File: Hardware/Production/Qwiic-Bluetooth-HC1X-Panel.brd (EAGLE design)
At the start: 97.3 x 97.3 mm, 492 parts, among them J1 ISP, J10 PIO, J11 ISP, J12 Qwiic-L, J13 Qwiic-R, J14 I2C, J15 PIO, J16 ISP, J17 Qwiic-L, J18 Qwiic-R, J19 I2C, J2 Qwiic-L, J20 PIO, J21 ISP, J22 Qwiic-L, J23 Qwiic-R, J24 I2C, J25 PIO, J26 ISP, J27 Qwiic-L, J28 Qwiic-R, J29 I2C, J3 Qwiic-R, J30 PIO, J31 ISP, J32 Qwiic-L, J33 Qwiic-R, J34 I2C, J35 PIO, J36 ISP, J37 Qwiic-L, J38 Qwiic-R, J39 I2C, J4 I2C, J40 PIO, J41 ISP, J42 Qwiic-L, J43 Qwiic-R, J44 I2C, J45 PIO, J5 PIO, J6 ISP, J7 Qwiic-L, J8 Qwiic-R, J9 I2C, U1 ATTiny85-Arduino, U10 ATTiny85-Arduino, U11 HM-17, U12 ATTiny85-Arduino, U13 HM-17, U14 ATTiny85-Arduino, U15 HM-17, U16 ATTiny85-Arduino, U17 HM-17, U18 ATTiny85-Arduino, U2 HM-17, U3 HM-17, U4 ATTiny85-Arduino, U5 HM-17, U6 ATTiny85-Arduino, U7 HM-17, U8 ATTiny85-Arduino, U9 HM-17

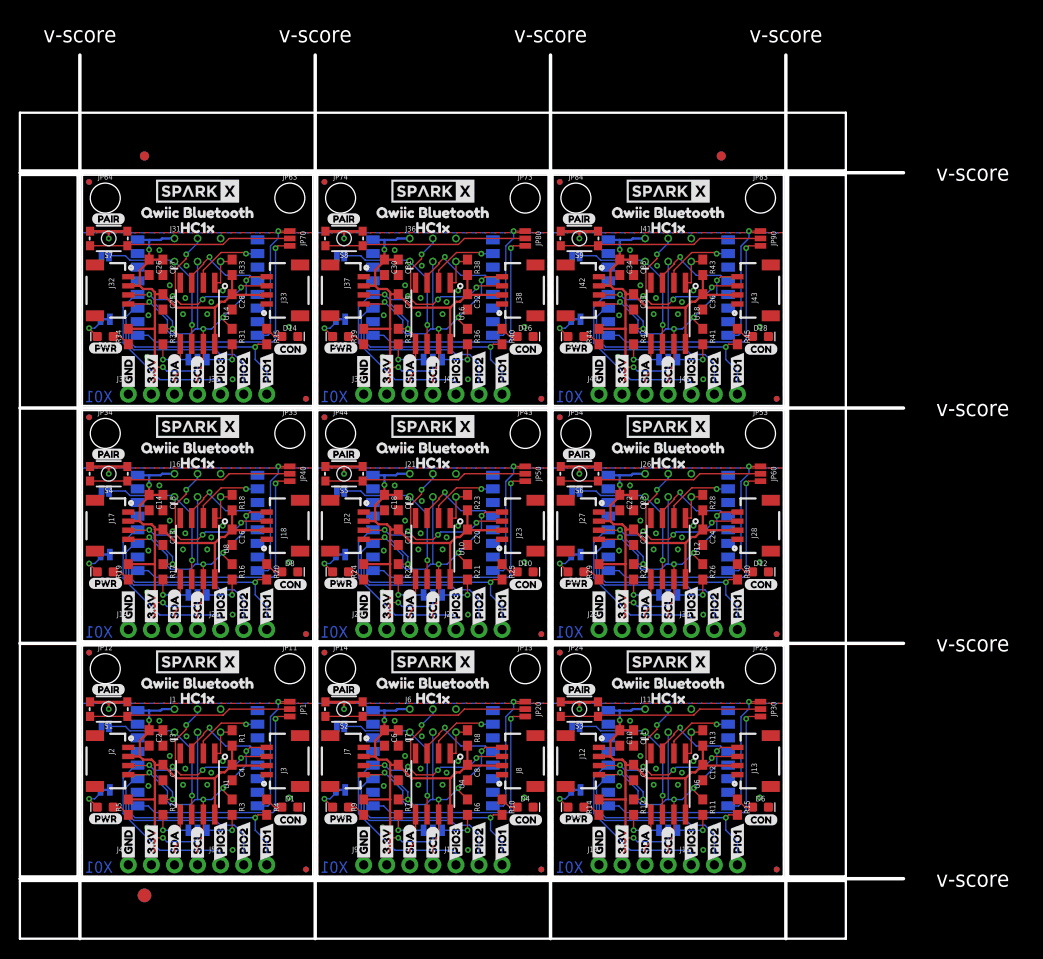
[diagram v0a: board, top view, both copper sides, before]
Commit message: Pushing production panel for x02.
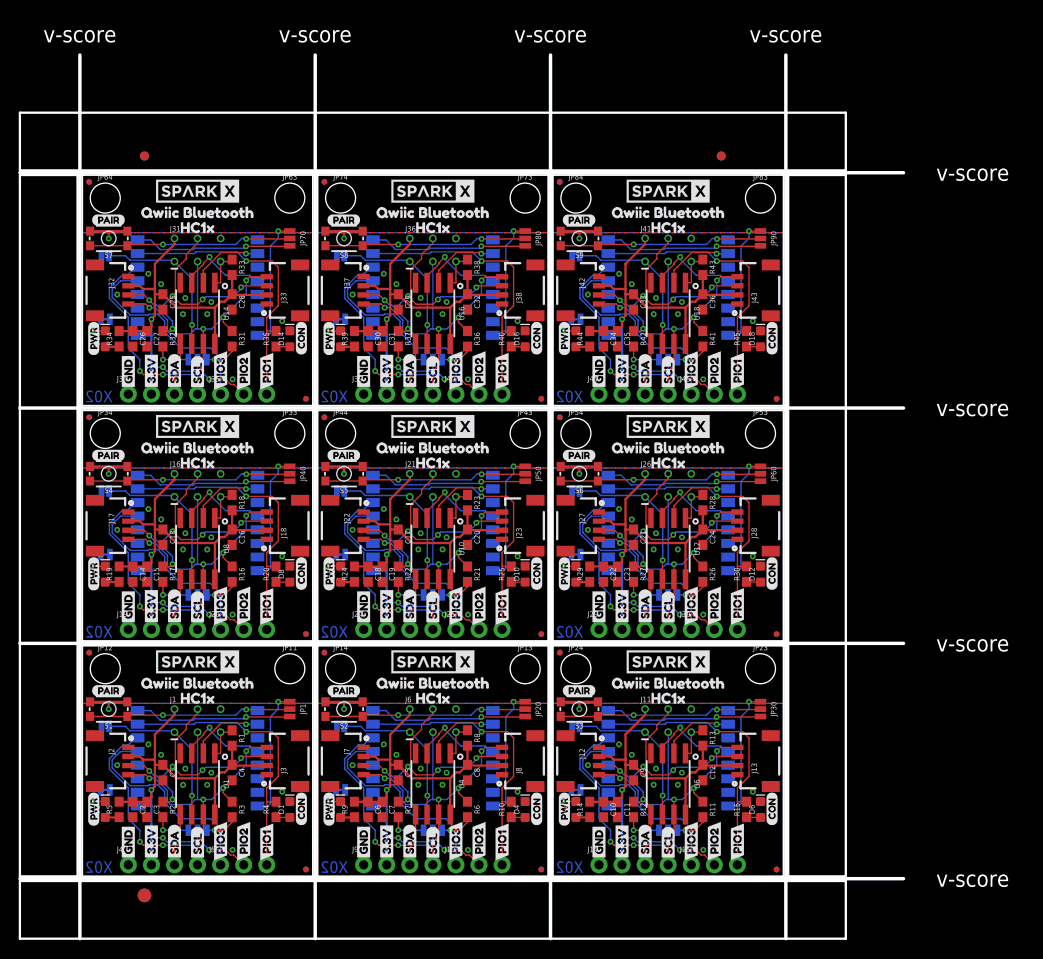
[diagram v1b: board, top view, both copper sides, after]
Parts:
- JP10, JP22, JP3, JP32, JP42, JP52, JP62, JP72, JP82: value JUMPER-SMT_3_2-NC_TRACE_NO-SILK -> I2C
- LOGO12, LOGO15, LOGO18, LOGO2, LOGO21, LOGO24, LOGO27, LOGO6, LOGO9: value SPARKX-LOGO3 -> SPARKX-LOGO4; device SparkX:SPARKX-SMALL -> SparkX:SPARKX-MEDIUM
- moved C18 8.07 mm to (31.5, 33.3)
- moved C23 8.07 mm to (58.9, 33.3)
- moved C11 8.07 mm to (58.9, 7.37)
- moved C14 8.07 mm to (5.59, 33.3)
- moved C15 8.07 mm to (7.11, 33.3)
- moved C19 8.07 mm to (33.0, 33.3)
- moved C22 8.07 mm to (57.4, 33.3)
- moved C3 8.07 mm to (7.11, 7.37)
- moved C6 8.07 mm to (31.5, 7.37)
- moved C10 8.07 mm to (57.4, 7.37)
- moved C2 8.07 mm to (5.59, 7.37)
- moved C7 8.07 mm to (33.0, 7.37)
- moved C26 8.07 mm to (5.59, 59.2)
- moved C27 8.07 mm to (7.11, 59.2)
- moved C30 8.07 mm to (31.5, 59.2)
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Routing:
- net PIO0/KEY-HM5: track 27.3 -> 17.4 mm
- net PIO0/KEY-HM4: track 27.3 -> 17.4 mm
- net PIO0/KEY-HM3: track 27.3 -> 17.4 mm
- net PIO0/KEY-HM1: track 27.3 -> 17.4 mm
- net PIO0/KEY-HM7: track 27.3 -> 17.4 mm
- net PIO0/KEY-HM11: track 27.3 -> 17.4 mm
- net PIO0/KEY-HM8: track 27.3 -> 17.4 mm
- net PIO0/KEY-HM6: track 27.3 -> 17.4 mm
- net PIO0/KEY-HM2: track 27.3 -> 17.4 mm
- net PIO1/LED2: track 24.0 -> 31.8 mm
- net PIO1/LED8: track 24.0 -> 31.8 mm
- net PIO1/LED5: track 24.0 -> 31.8 mm
- net PIO1/LED6: track 24.0 -> 31.8 mm
- net PIO1/LED3: track 24.0 -> 31.8 mm
- net PIO1/LED: track 24.0 -> 31.8 mm
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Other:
- board text added: "X02"
- board text removed: "X01"
